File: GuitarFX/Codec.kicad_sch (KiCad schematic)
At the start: 77 parts, among them IC401 PCM3060PWR, J401 Screw_Terminal_01x04, U1 CS4272, U401 TLV9161IDBVR, U402 TLV9161IDBVR, U404 TLV9161IDBVR, U405 TLV9161IDBVR

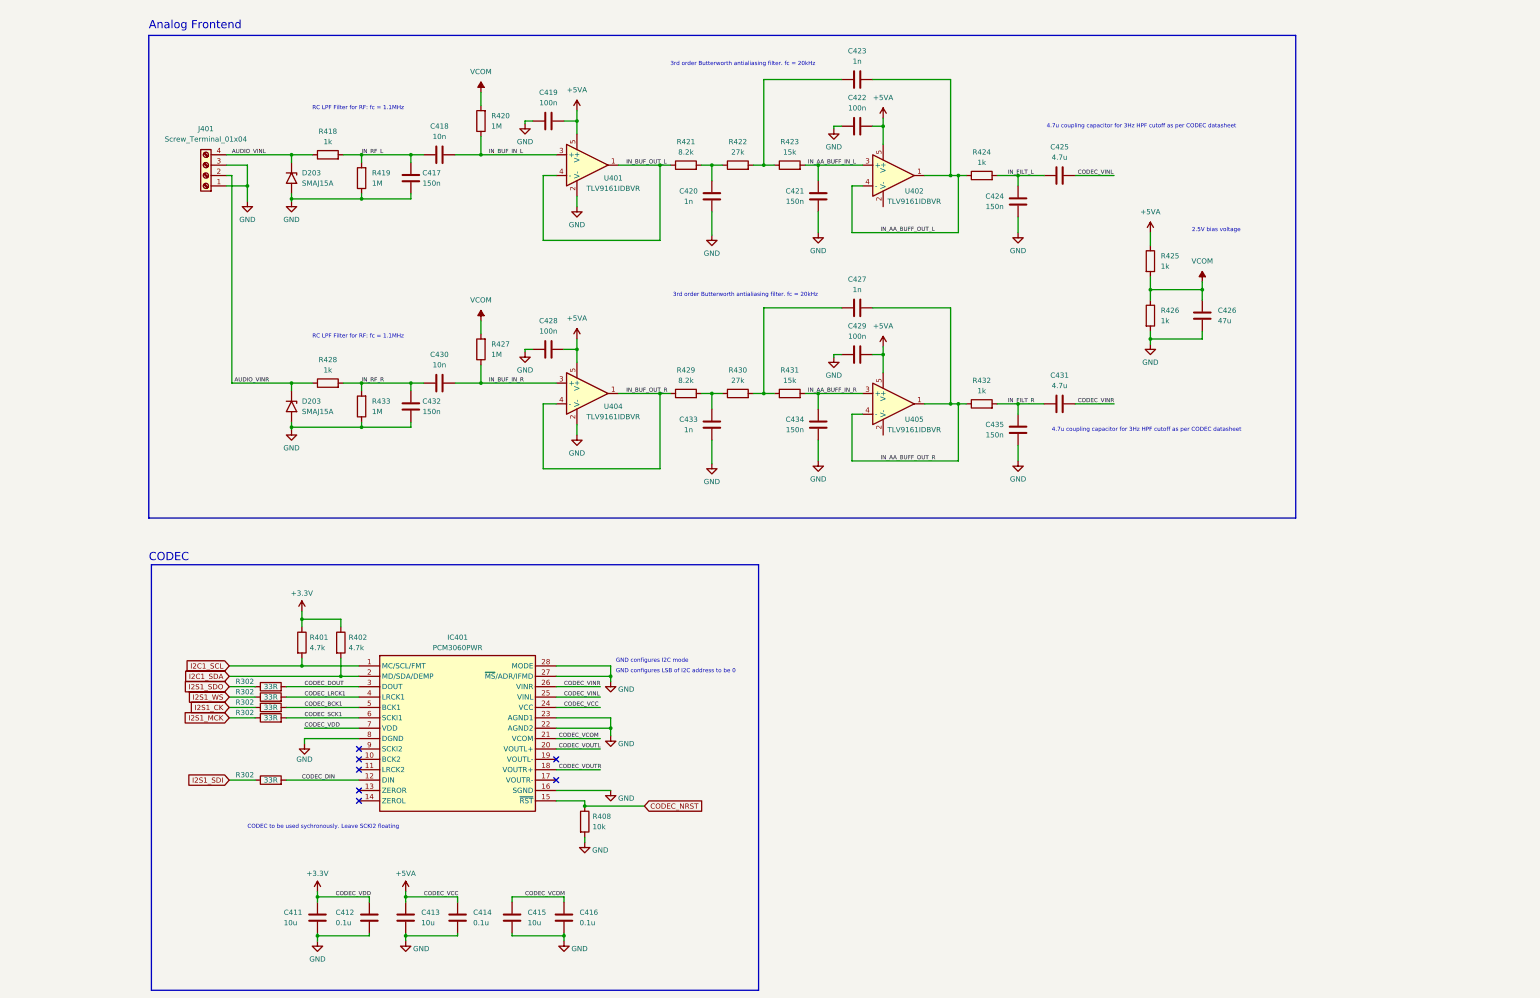
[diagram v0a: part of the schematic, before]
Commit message: Fixed capactor value on frontend
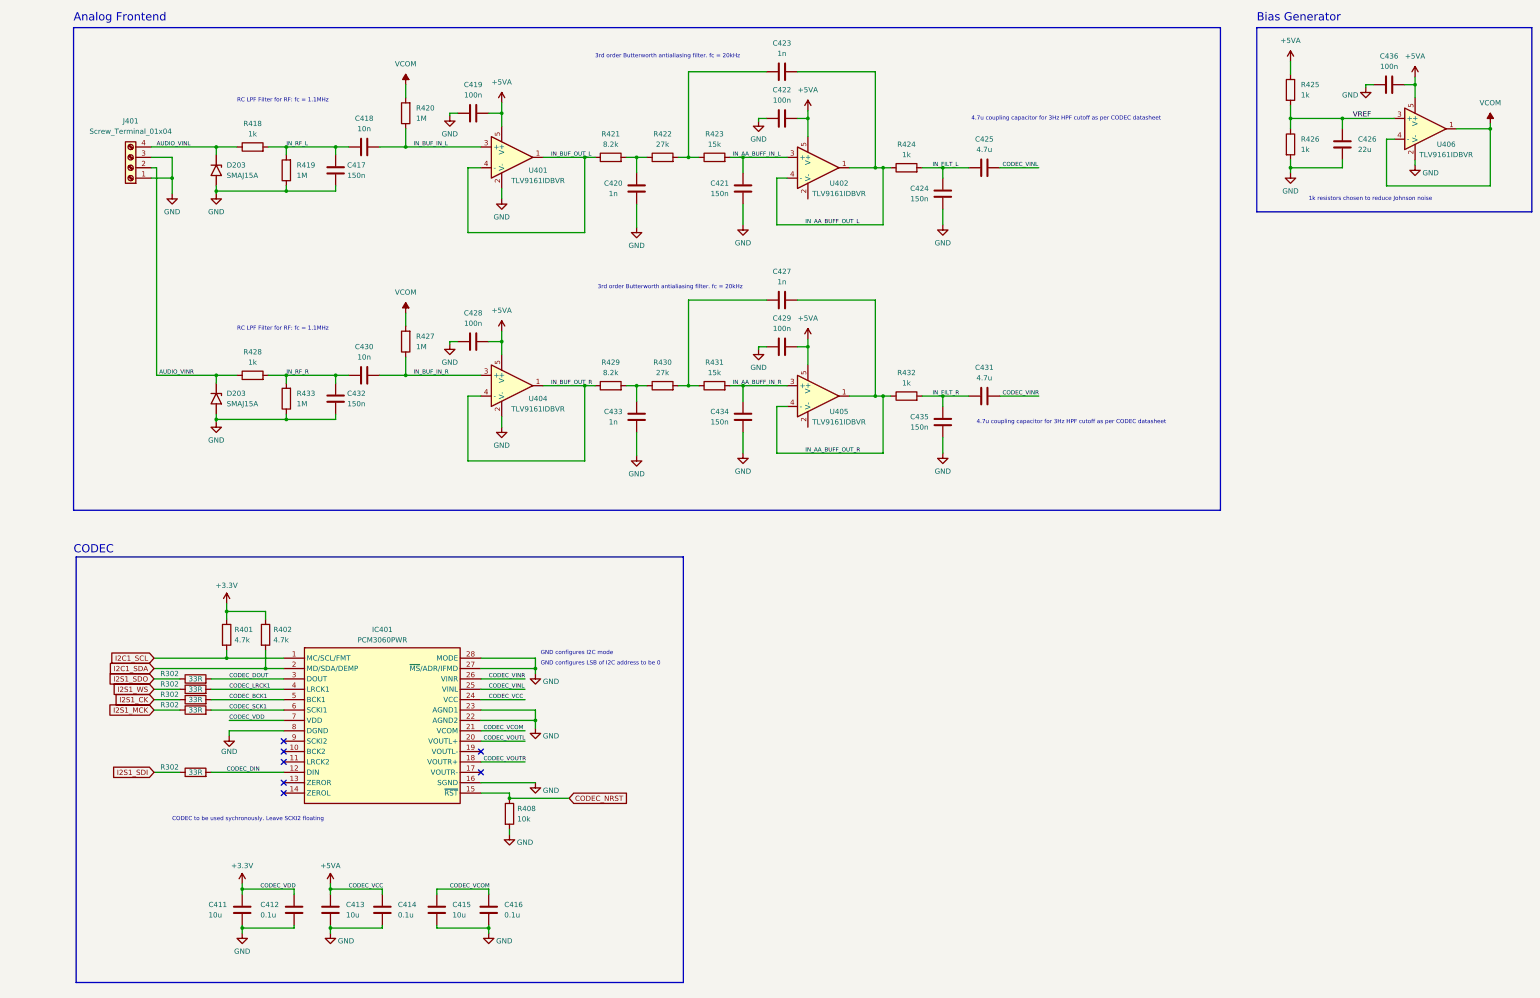
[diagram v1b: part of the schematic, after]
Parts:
- added C436: 100n, symbol Device:C
- added U406: TLV9161IDBVR, SOT95P280X145-5N, symbol TLV9161IDBVR:TLV9161IDBVR
- C426: value 47u -> 22u
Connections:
- net +5VA: now also C436.1, U406.5 (V+)
- net GND: now also C436.2, U406.2 (V-)
- net VCOM: now also U406.1, U406.4 (-); no longer C426.1, R425.2, R426.1
- new net VREF: C426.1, R425.2, R426.1, U406.3 (+)
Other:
- note added: "1k resistors chosen to reduce Johnson noise"
- note added: "Bias Generator"
- note removed: "2.5V bias voltage"
- moved on the sheet: C411, C412, C413, C414, C415, C416, C417, C418, C419, C420, C421, C422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

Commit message: Completed the 'Rearend' lmao
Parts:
- removed C401, C404, C405, C407, C409: 100n, symbol Device:C
- removed C402, C403, C406, C408: 1u, symbol Device:C
- removed C410: 47u, symbol Device:C
- removed R302 (x5): 33R, symbol Device:R
- removed R409, R417: 10k, symbol Device:R
- removed R415, R416: 4.7k, symbol Device:R
- removed U1: CS4272, Package_SO:TSSOP-28_4.4x9.7mm_P0.65mm, symbol Audio:CS4272
- added C437, C442, C443: 100n, symbol Device:C
- added C438, C441, C445: 1n, symbol Device:C
- added C439, C446: 150p, symbol Device:C
- added C440, C444: 4.7u, symbol Device:C
- added D203 (x2): SMAJ15A, Diode_SMD:D_SMA, symbol Diode:SMAJ15A
- added R434, R439: 8.2k, symbol Device:R
- added R435, R440: 27k, symbol Device:R
- added R436, R441: 15k, symbol Device:R
- added R437, R442: 100R, symbol Device:R
- added R438, R443: 10k, symbol Device:R
- added U407, U408, U409, U410: TLV9161IDBVR, SOT95P280X145-5N, symbol TLV9161IDBVR:TLV9161IDBVR
- C417, C421, C432, C434: value 150n -> 150p
- C424: value 150n -> 100n
- C435: value 150n -> 1n
- R424, R432: value 1k -> 100R
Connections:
- net +5VA: now also C424.1, C437.1, C442.1, C443.1, U407.5 (V+), U408.5 (V+), U409.5 (V+), U410.5 (V+)
- net CODEC_VOUTL: now also U407.3 (+)
- net CODEC_VOUTR: now also U409.3 (+)
- net GND: now also U402.2 (V-), U405.2 (V-), C437.2, C438.2, C439.2, C442.2, C443.2, C445.2, C446.2, D203.2 (A2), D203.2 (A2), R438.1, R443.1, U407.2 (V-), U408.2 (V-), U409.2 (V-), U410.2 (V-); no longer C435.2
- net IN_FILT_L: no longer names the net of C425.2, R424.2
- net IN_FILT_L: no longer C424.1
- net IN_FILT_R: no longer names the net of C431.2, R432.2
- net IN_FILT_R: no longer C435.1
- new net: C438.1, R434.2, R435.1
- new net: C440.2, R437.2
- new net: C435.2, R435.2, R436.1
- new net: C444.2, R442.2
- new net: R439.1, U409.1, U409.4 (-)
- new net: C445.1, R439.2, R440.1
- new net: C441.2, R440.2, R441.1
- new net: R434.1, U407.1, U407.4 (-)
- new net AUDIO_VOUTL: C440.1, D203.1 (A1), R438.2
- new net AUDIO_VOUTR: C444.1, D203.1 (A1), R443.2
- new net OUT_AA_BUFF_IN_L: C439.1, R436.2, U408.3 (+)
- new net OUT_AA_BUFF_IN_R: C446.1, R441.2, U410.3 (+)
- new net OUT_AA_BUFF_OUT_L: C435.1, R437.1, U408.1, U408.4 (-)
- new net OUT_AA_BUFF_OUT_R: C441.1, R442.1, U410.1, U410.4 (-)
- no-connect marks 8 -> 7
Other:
- note added: "ADC input impedance is 10k"
- note added: "Analog Rearend, lmao"
- note added: "Output from DAC is DC Coupled (No need for biasing pullup)"
- note added: "Rin = 500k (Parallel 1M resistors)"
- note removed: "Use MCLK from MCU No XTL required"
- note removed: "Using pulldown resistor to assert low before mcu firmware boots"
- moved on the sheet: C411, C412, C413, C414, C415, C416, C417, C418, C419, C420, C421, C422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

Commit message: Got rid of most ERC violations
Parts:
- removed U401, U410: TLV9161IDBVR, SOT95P280X145-5N, symbol TLV9161IDBVR:TLV9161IDBVR
- added U403, U406: TLV9161IDBVR, SOT95P280X145-5N, symbol TLV9161IDBVR:TLV9161IDBVR
- renumbered C423 to C401, C436 to C402, C419 to C403, C422 to C404, C426 to C405, C418 to C406, C425 to C407, C417 to C408, C420 to C409, C421 to C410, C427 to C411, C428 to C412, C429 to C413, C430 to C414, C431 to C415, C432 to C416, C433 to C417, C434 to C418, C435 to C419, C424 to C420, C437 to C421, C440 to C422, C438 to C423, C439 to C424, C441 to C425, C442 to C426, C443 to C427, C411 to C428, C412 to C429, C413 to C430, C414 to C431, C415 to C432, C416 to C433, C444 to C434, C445 to C435, C446 to C436, R425 to R401, R420 to R402, R426 to R403, R418 to R404, R421 to R405, R422 to R406, R423 to R407, R424 to R408, R419 to R409, R427 to R410, R428 to R411, R429 to R412, R430 to R413, R431 to R414, R432 to R415, R433 to R416, R401 to R417, R402 to R418, R434 to R421, R435 to R422, R436 to R423, R437 to R425, R438 to R427, R408 to R429, R439 to R430, R440 to R431, R441 to R432, R442 to R433, R443 to R434, U406 to U401
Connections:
- net +5VA: now also U403.5 (V+), U406.5 (V+)
- net CODEC_VOUTL: now also U406.3 (+); no longer U407.3 (+)
- net CODEC_VOUTR: now also U408.3 (+); no longer U409.3 (+)
- net GND: now also U403.2 (V-), U406.2 (V-)
- net IN_AA_BUFF_IN_L: now also U403.3 (+); no longer U402.3 (+)
- net IN_AA_BUFF_OUT_L: now also U403.1, U403.4 (-); no longer U402.1, U402.4 (-)
- net IN_BUF_IN_L: now also U402.3 (+)
- net IN_BUF_OUT_L: now also U402.1, U402.4 (-)
- net OUT_AA_BUFF_IN_L: now also U407.3 (+); no longer U408.3 (+)
- net OUT_AA_BUFF_IN_R: now also U409.3 (+)
- net OUT_AA_BUFF_OUT_L: now also U407.1, U407.4 (-); no longer U408.1, U408.4 (-)
- net OUT_AA_BUFF_OUT_R: now also U409.1, U409.4 (-)
- new net: R430.1, U408.1, U408.4 (-)
- new net: R421.1, U406.1, U406.4 (-)
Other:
- note added: "CODEC VCC"
- note added: "CODEC VDD"

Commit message: Updated footprints for capacitors
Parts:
- C401, C402, C403, C404, C406, C408, C409, C410, C411, C412, C413, C414, C416, C417, C418, C419, C420, C421, C423, C424, C425, C426, C427, C429, C431, C433, C435, C436: footprint (none) -> Capacitor_SMD:C_0402_1005Metric
- C405: footprint (none) -> Capacitor_SMD:C_0805_2012Metric
- C407, C415, C422, C428, C430, C432, C434: footprint (none) -> Capacitor_SMD:C_0603_1608Metric
- U401, U402, U403, U404, U405, U406, U407, U408, U409: footprint SOT95P280X145-5N -> TLV9161IDBVR:SOT95P280X145-5N

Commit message: Created RGB LED footprint
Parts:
- IC401: footprint SOP65P640X120-28N -> (none)
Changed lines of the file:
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@@
       (effects (font (size 1.27 1.27)))
     )
-    (property "Footprint" "SOP65P640X120-28N" (at 351.155 265.735 0)
+    (property "Footprint" "" (at 351.155 265.735 0)
       (effects (font (size 1.27 1.27)) (justify left top) hide)
     )

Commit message: Assigned all footprints
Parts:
- IC401: footprint (none) -> PCM3060PWR:SOP65P640X120-28N
- J401: footprint (none) -> TerminalBlock_Phoenix:TerminalBlock_Phoenix_MPT-0,5-4-2.54_1x04_P2.54mm_Horizontal
- R302, R417, R418: footprint (none) -> Resistor_SMD:R_0603_1608Metric
- R401, R402, R403, R404, R405, R406, R407, R408, R409, R410, R411, R412, R413, R414, R415, R416, R421, R422, R423, R425, R427, R429, R430, R431, R432, R433, R434: footprint (none) -> Resistor_SMD:R_0402_1005Metric
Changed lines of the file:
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@@
       (effects (font (size 1.27 1.27)))
     )
-    (property "Footprint" "" (at 219.71 55.753 90)
+    (property "Footprint" "Resistor_SMD:R_0402_1005Metric" (at 219.71 55.753 90)
       (effects (font (size 1.27 1.27)) hide)
     )
@@
       (effects (font (size 1.27 1.27)))
     )
-    (property "Footprint" "" (at 172.72 53.213 90)
+    (property "Footprint" "Resistor_SMD:R_0402_1005Metric" (at 172.72 53.213 90)
       (effects (font (size 1.27 1.27)) hide)
     )
@@
       (effects (font (size 1.27 1.27)) (justify right))
     )
-    (property "Footprint" "" (at 98.933 96.52 90)
+    (property "Footprint" "Resistor_SMD:R_0402_1005Metric" (at 98.933 96.52 90)
       (effects (font (size 1.27 1.27)) hide)
     )
@@
       (effects (font (size 1.27 1.27)))
     )
-    (property "Footprint" "" (at 285.115 177.673 90)
+    (property "Footprint" "Resistor_SMD:R_0603_1608Metric" (at 285.115 177.673 90)
       (effects (font (size 1.27 1.27)) hide)
     )
@@
       (effects (font (size 1.27 1.27)))
     )
-    (property "Footprint" "" (at 285.115 182.753 90)
+    (property "Footprint" "Resistor_SMD:R_0603_1608Metric" (at 285.115 182.753 90)
       (effects (font (size 1.27 1.27)) hide)
     )
@@
       (effects (font (size 1.27 1.27)) (justify left))
     )
-    (property "Footprint" "" (at 290.957 165.1 90)
+    (property "Footprint" "Resistor_SMD:R_0603_1608Metric" (at 290.957 165.1 90)
       (effects (font (size 1.27 1.27)) hide)
     )
@@
       (effects (font (size 1.27 1.27)) (justify left))
     )
-    (property "Footprint" "" (at 300.482 165.1 90)
+    (property "Footprint" "Resistor_SMD:R_0603_1608Metric" (at 300.482 165.1 90)
       (effects (font (size 1.27 1.27)) hide)
     )
@@
       (effects (font (size 1.27 1.27)) (justify right))
     )
-    (property "Footprint" "" (at 204.343 241.3 90)
+    (property "Footprint" "Resistor_SMD:R_0402_1005Metric" (at 204.343 241.3 90)
       (effects (font (size 1.27 1.27)) hide)
     )
@@
       (effects (font (size 1.27 1.27)))
     )
-    (property "Footprint" "" (at 351.155 265.735 0)
+    (property "Footprint" "PCM3060PWR:SOP65P640X120-28N" (at 351.155 265.735 0)
       (effects (font (size 1.27 1.27)) (justify left top) hide)
     )
@@
       (effects (font (size 1.27 1.27)) (justify left))
     )
-    (property "Footprint" "" (at 282.702 34.925 90)
+    (property "Footprint" "Resistor_SMD:R_0402_1005Metric" (at 282.702 34.925 90)
       (effects (font (size 1.27 1.27)) hide)
     )
@@
       (effects (font (size 1.27 1.27)) (justify right))
     )
-    (property "Footprint" "" (at 69.723 54.61 90)
+    (property "Footprint" "Resistor_SMD:R_0402_1005Metric" (at 69.723 54.61 90)
       (effects (font (size 1.27 1.27)) hide)
     )
@@
       (effects (font (size 1.27 1.27)))
     )
-    (property "Footprint" "" (at 179.705 183.388 90)
+    (property "Footprint" "Resistor_SMD:R_0402_1005Metric" (at 179.705 183.388 90)
       (effects (font (size 1.27 1.27)) hide)
     )
@@
       (effects (font (size 1.27 1.27)) (justify left))
     )
-    (property "Footprint" "" (at 282.702 48.26 90)
+    (property "Footprint" "Resistor_SMD:R_0402_1005Metric" (at 282.702 48.26 90)
       (effects (font (size 1.27 1.27)) hide)
     )
@@
       (effects (font (size 1.27 1.27)))
     )
-    (property "Footprint" "" (at 160.02 109.093 90)
+    (property "Footprint" "Resistor_SMD:R_0402_1005Metric" (at 160.02 109.093 90)
       (effects (font (size 1.27 1.27)) hide)
     )
@@
       (effects (font (size 1.27 1.27)))
     )
-    (property "Footprint" "" (at 160.02 53.213 90)
+    (property "Footprint" "Resistor_SMD:R_0402_1005Metric" (at 160.02 53.213 90)
       (effects (font (size 1.27 1.27)) hide)
     )
@@
       (effects (font (size 1.27 1.27)))
     )
-    (property "Footprint" "" (at 219.71 111.633 90)
+    (property "Footprint" "Resistor_SMD:R_0402_1005Metric" (at 219.71 111.633 90)
       (effects (font (size 1.27 1.27)) hide)
     )
@@
       (effects (font (size 1.27 1.27)))
     )
-    (property "Footprint" "" (at 179.705 236.728 90)
+    (property "Footprint" "Resistor_SMD:R_0402_1005Metric" (at 179.705 236.728 90)
       (effects (font (size 1.27 1.27)) hide)
     )
@@
       (effects (font (size 1.27 1.27)) (justify right))
     )
-    (property "Footprint" "" (at 69.723 110.49 90)
+    (property "Footprint" "Resistor_SMD:R_0402_1005Metric" (at 69.723 110.49 90)
       (effects (font (size 1.27 1.27)) hide)
     )
@@
       (effects (font (size 1.27 1.27)))
     )
-    (property "Footprint" "" (at 106.045 234.188 90)
+    (property "Footprint" "Resistor_SMD:R_0402_1005Metric" (at 106.045 234.188 90)
       (effects (font (size 1.27 1.27)) hide)
     )
@@
       (effects (font (size 1.27 1.27)))
     )
-    (property "Footprint" "" (at 29.845 53.975 0)
+    (property "Footprint" "TerminalBlock_Phoenix:TerminalBlock_Phoenix_MPT-0,5-4-2.54_1x04_P2.54mm_Horizontal" (at 29.845 53.975 0)
       (effects (font (size 1.27 1.27)) hide)
     )
@@
       (effects (font (size 1.27 1.27)))
     )
-    (property "Footprint" "" (at 59.69 50.673 90)
+    (property "Footprint" "Resistor_SMD:R_0402_1005Metric" (at 59.69 50.673 90)
       (effects (font (size 1.27 1.27)) hide)
     )
@@
       (effects (font (size 1.27 1.27)))
     )
-    (property "Footprint" "" (at 147.32 53.213 90)
+    (property "Footprint" "Resistor_SMD:R_0402_1005Metric" (at 147.32 53.213 90)
       (effects (font (size 1.27 1.27)) hide)
     )
@@
       (effects (font (size 1.27 1.27)) (justify right))
     )
-    (property "Footprint" "" (at 204.343 187.96 90)
+    (property "Footprint" "Resistor_SMD:R_0402_1005Metric" (at 204.343 187.96 90)
       (effects (font (size 1.27 1.27)) hide)
     )
@@
       (effects (font (size 1.27 1.27)))
     )
-    (property "Footprint" "" (at 285.115 200.533 90)
+    (property "Footprint" "Resistor_SMD:R_0603_1608Metric" (at 285.115 200.533 90)
       (effects (font (size 1.27 1.27)) hide)
     )
@@
       (effects (font (size 1.27 1.27)))
     )
-    (property "Footprint" "" (at 147.32 109.093 90)
+    (property "Footprint" "Resistor_SMD:R_0402_1005Metric" (at 147.32 109.093 90)
       (effects (font (size 1.27 1.27)) hide)
     )
@@
       (effects (font (size 1.27 1.27)) (justify left))
     )
-    (property "Footprint" "" (at 360.172 208.915 90)
+    (property "Footprint" "Resistor_SMD:R_0402_1005Metric" (at 360.172 208.915 90)
       (effects (font (size 1.27 1.27)) hide)
     )
@@
       (effects (font (size 1.27 1.27)))
     )
-    (property "Footprint" "" (at 118.745 234.188 90)
+    (property "Footprint" "Resistor_SMD:R_0402_1005Metric" (at 118.745 234.188 90)
       (effects (font (size 1.27 1.27)) hide)
     )
@@
       (effects (font (size 1.27 1.27)))
     )
-    (property "Footprint" "" (at 106.045 180.848 90)
+    (property "Footprint" "Resistor_SMD:R_0402_1005Metric" (at 106.045 180.848 90)
       (effects (font (size 1.27 1.27)) hide)
     )
@@
       (effects (font (size 1.27 1.27)))
     )
-    (property "Footprint" "" (at 131.445 234.188 90)
+    (property "Footprint" "Resistor_SMD:R_0402_1005Metric" (at 131.445 234.188 90)
       (effects (font (size 1.27 1.27)) hide)
     )
@@
       (effects (font (size 1.27 1.27)))
     )
-    (property "Footprint" "" (at 118.745 180.848 90)
+    (property "Footprint" "Resistor_SMD:R_0402_1005Metric" (at 118.745 180.848 90)
       (effects (font (size 1.27 1.27)) hide)
     )
@@
       (effects (font (size 1.27 1.27)))
     )
-    (property "Footprint" "" (at 172.72 109.093 90)
+    (property "Footprint" "Resistor_SMD:R_0402_1005Metric" (at 172.72 109.093 90)
       (effects (font (size 1.27 1.27)) hide)
     )
@@
       (effects (font (size 1.27 1.27)))
     )
-    (property "Footprint" "" (at 285.115 185.293 90)
+    (property "Footprint" "Resistor_SMD:R_0603_1608Metric" (at 285.115 185.293 90)
       (effects (font (size 1.27 1.27)) hide)
     )
@@
       (effects (font (size 1.27 1.27)))
     )
-    (property "Footprint" "" (at 59.69 106.553 90)
+    (property "Footprint" "Resistor_SMD:R_0402_1005Metric" (at 59.69 106.553 90)
       (effects (font (size 1.27 1.27)) hide)
     )
@@
       (effects (font (size 1.27 1.27)) (justify right))
     )
-    (property "Footprint" "" (at 98.933 40.64 90)
+    (property "Footprint" "Resistor_SMD:R_0402_1005Metric" (at 98.933 40.64 90)
       (effects (font (size 1.27 1.27)) hide)
     )
@@
       (effects (font (size 1.27 1.27)))
     )
-    (property "Footprint" "" (at 285.115 180.213 90)
+    (property "Footprint" "Resistor_SMD:R_0603_1608Metric" (at 285.115 180.213 90)
       (effects (font (size 1.27 1.27)) hide)
     )
@@
       (effects (font (size 1.27 1.27)))
     )
-    (property "Footprint" "" (at 131.445 180.848 90)
+    (property "Footprint" "Resistor_SMD:R_0402_1005Metric" (at 131.445 180.848 90)
       (effects (font (size 1.27 1.27)) hide)
     )
